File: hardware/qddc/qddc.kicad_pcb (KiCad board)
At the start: 2 copper layers, 37 parts, among them IC1 FST3253MTCX, IC2 OPA2350UA, J1 In_cos, J2 In_sin, J3 In_RF, J4 PWR, J5 Out_I, J6 Out_Q, T1 ETC4-1-2TR

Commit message: PCB for Quad DDC
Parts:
- C4: moved to B.Cu
- moved J5 20.3 mm to (164.5, 94.6)
- moved J6 20.3 mm to (164.5, 112.4)
- moved R10 17.2 mm to (123.8, 113.0), turned to 90 degrees
- moved R14 16.5 mm to (133.3, 111.8), turned to 90 degrees
- moved C10 15.6 mm to (135.9, 111.8), turned to 270 degrees
- moved C6 15.2 mm to (120.7, 113.0)
- moved J2 13.5 mm to (114.9, 86.4)
- moved R2 13.5 mm to (114.9, 93.3)
- moved J1 13.5 mm to (134.0, 86.4)
- moved R1 13.5 mm to (134.0, 93.3)
- moved R8 13.4 mm to (127.6, 97.8), turned to 270 degrees
- moved C5 11.5 mm to (124.5, 97.8), turned to 270 degrees
- moved L1 9.67 mm to (119.4, 123.2)
- moved C12 9.53 mm to (156.2, 94.6), turned to 180 degrees
- moved C13 9.53 mm to (156.2, 112.4)
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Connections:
- IC2 pad 6: Net-(C10-Pad2) -> Net-(C10-Pad1)
- IC2 pad 7: Net-(C10-Pad1) -> Net-(C10-Pad2)
- J4 pad 1: PTT -> GND
- J4 pad 4: GND -> PTT
- R10 pad 1: Net-(C10-Pad2) -> Net-(C10-Pad1)
- R13 pad 2: Net-(C10-Pad1) -> Net-(C10-Pad2)
- R14 pad 1: Net-(C10-Pad1) -> Net-(C10-Pad2)
- R14 pad 2: Net-(C10-Pad2) -> Net-(C10-Pad1)
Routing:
- net PTT: track 0.00 -> 32.0 mm, vias 0 -> 3
- net VCC: track 0.00 -> 31.3 mm, vias 0 -> 2
- net Net-(C8-Pad1): track 0.00 -> 28.7 mm
- net VAA: track 0.00 -> 27.0 mm, vias 0 -> 2
- net Net-(C9-Pad2): track 0.00 -> 26.9 mm
- net Net-(C10-Pad1): track 0.00 -> 23.7 mm
- net Net-(C10-Pad2): track 0.00 -> 23.0 mm
- net Net-(C5-Pad2): track 0.00 -> 21.8 mm
- net Net-(C1-Pad1): track 0.00 -> 21.8 mm
- net Net-(C6-Pad1): track 0.00 -> 21.7 mm
- net Net-(C7-Pad2): track 0.00 -> 21.3 mm, vias 0 -> 2
- net Net-(J3-Pad2): track 0.00 -> 21.1 mm, vias 0 -> 2
- net Net-(IC1-Pad2): track 0.00 -> 18.6 mm, vias 0 -> 2
- net Net-(IC1-Pad14): track 0.00 -> 18.0 mm, vias 0 -> 2
- net Net-(C9-Pad1): track 0.00 -> 11.4 mm
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- added copper zone on B.Cu, net GND
- added copper zone on F.Cu, net GND
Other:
- board outline added: 71.1 x 46.4 mm

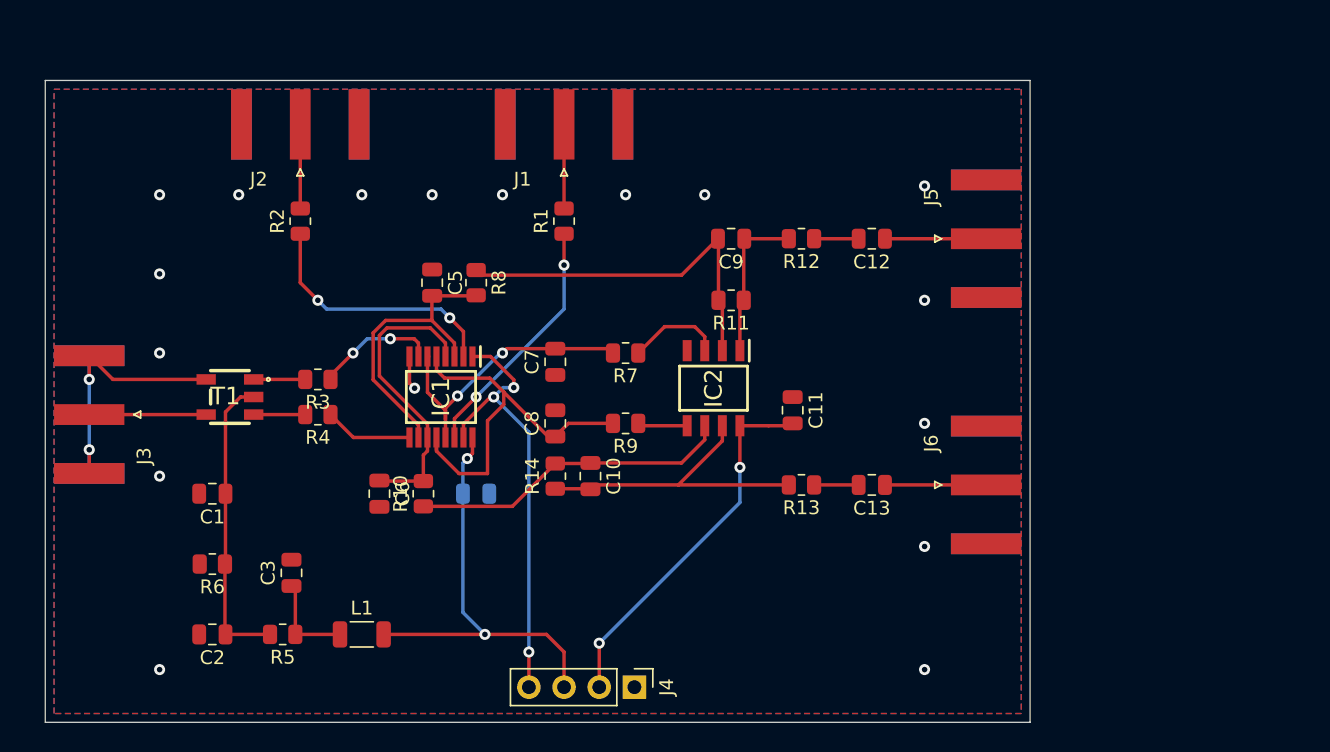
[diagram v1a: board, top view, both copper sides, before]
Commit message: Done PCB for Quad DDC
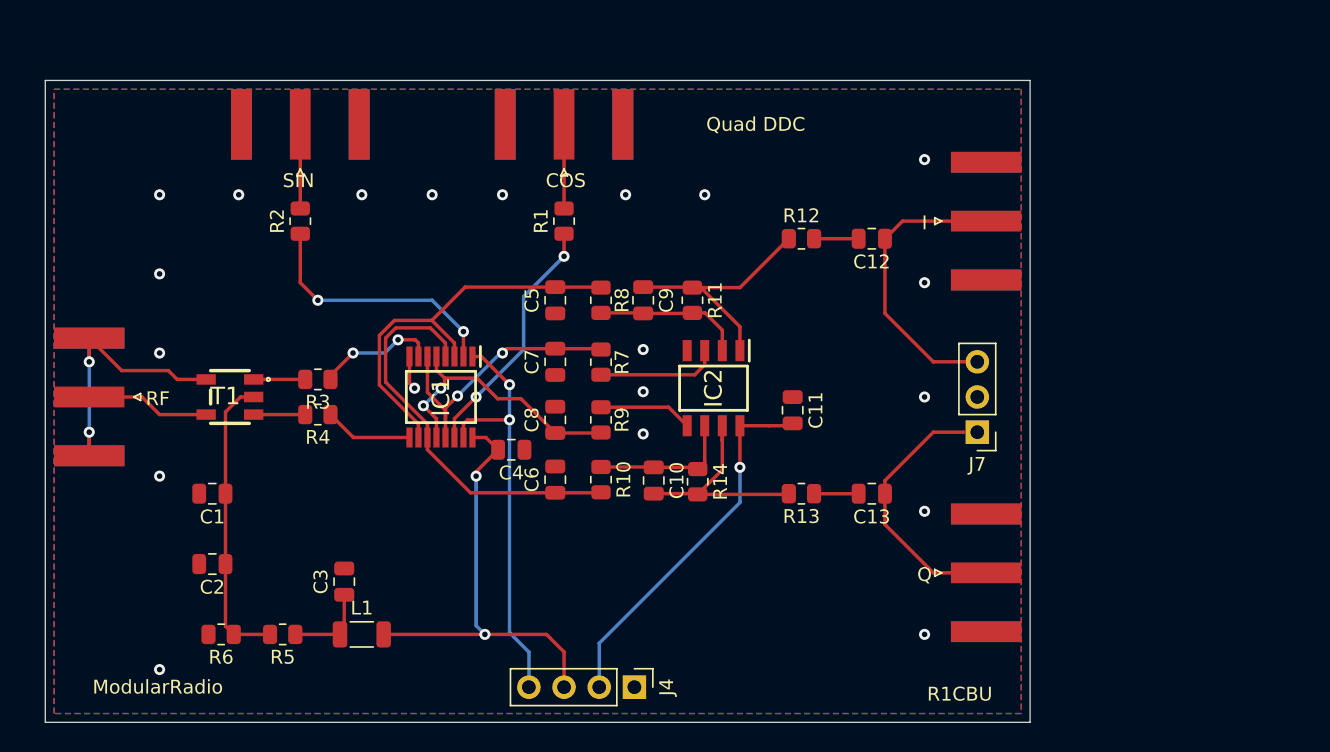
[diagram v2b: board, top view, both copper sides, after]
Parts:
- added J7: Conn_01x03_Male, Connector_PinHeader_2.54mm:PinHeader_1x03_P2.54mm_Vertical, F.Cu at (163.8, 108.6)
- C4: moved to F.Cu
- moved R10 12.9 mm to (136.7, 112.0), turned to 270 degrees
- moved C6 12.7 mm to (133.3, 112.0), turned to 90 degrees
- moved R14 10.3 mm to (143.6, 112.2)
- moved R8 9.11 mm to (136.7, 99.1), turned to 90 degrees
- moved C5 8.98 mm to (133.3, 99.1), turned to 90 degrees
- moved C9 7.75 mm to (139.7, 99.1), turned to 270 degrees
- moved Q 6.35 mm to (164.5, 118.7)
- moved R6 5.12 mm to (109.2, 123.2)
- moved C2 5.08 mm to (108.6, 118.1)
- moved C10 4.58 mm to (140.5, 112.1)
- moved C4 4.07 mm to (130.2, 109.9)
- moved C3 3.86 mm to (118.1, 119.4)
- moved R11 2.79 mm to (143.3, 99.1), turned to 270 degrees
- moved R7 1.90 mm to (136.7, 103.5), turned to 90 degrees
- moved R9 1.80 mm to (136.7, 107.7), turned to 270 degrees
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- renumbered J1 to COS, J5 to I, J6 to Q, J3 to RF, J2 to SIN
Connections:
- R12 pad 1: Net-(C12-Pad2) -> Net-(C9-Pad1)
- R12 pad 2: Net-(C9-Pad1) -> Net-(C12-Pad2)
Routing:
- net Net-(C9-Pad2): track 26.9 -> 10.8 mm
- net Net-(C12-Pad1): track 7.31 -> 21.3 mm
- net Net-(C10-Pad1): track 23.7 -> 10.8 mm
- net Net-(C13-Pad1): track 7.31 -> 20.0 mm
- net Net-(C8-Pad1): track 28.7 -> 20.1 mm, vias 0 -> 2
- net Net-(C6-Pad1): track 21.7 -> 29.2 mm
- net Net-(C5-Pad2): track 21.8 -> 29.3 mm
- net Net-(C9-Pad1): track 11.4 -> 18.3 mm
- net Net-(C10-Pad2): track 23.0 -> 16.6 mm
- net Net-(IC2-Pad5): track 3.85 -> 7.02 mm
- net Net-(IC2-Pad3): track 6.90 -> 8.81 mm
- net PTT: track 32.0 -> 30.4 mm, vias 3 -> 2
- net VCC: track 31.3 -> 32.6 mm
- net Net-(C7-Pad2): track 21.3 -> 20.3 mm
- net Net-(C3-Pad1): track 6.84 -> 6.21 mm
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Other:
- board text added: "ModularRadio"
- board text added: "Quad DDC"
- board text added: "R1CBU"

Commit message: Optimize Quad DDC, Gerber files
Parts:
- removed I: Out_I, Connector_Coaxial:SMA_Amphenol_132289_EdgeMount
- removed Q: Out_Q, Connector_Coaxial:SMA_Amphenol_132289_EdgeMount
- removed the RF at (99.7, 106.0)
- added RF: In_RF, kicad:RFSOLUTIONS_CON-SMA-EDGE-S, F.Cu at (104.1, 104.6)
- Cos: renamed from COS; footprint Connector_Coaxial:SMA_Amphenol_132289_EdgeMount -> kicad:RFSOLUTIONS_CON-SMA-EDGE-S
- Sin: renamed from SIN; footprint Connector_Coaxial:SMA_Amphenol_132289_EdgeMount -> kicad:RFSOLUTIONS_CON-SMA-EDGE-S
- moved R6 22.7 mm to (111.8, 100.6)
- moved Out 10.8 mm to (153.0, 108.0)
- moved L1 9.73 mm to (125.7, 115.8)
- moved R5 8.02 mm to (116.8, 115.8)
- moved Cos 7.91 mm to (126.5, 88.9), turned to 270 degrees
- moved PWR 7.63 mm to (138.7, 119.4)
- moved R1 7.52 mm to (126.5, 94.0)
- moved C12 5.85 mm to (151.8, 98.4)
- moved R12 5.39 mm to (147.3, 98.4)
- moved C3 5.12 mm to (120.7, 114.9)
- moved C13 4.45 mm to (151.8, 113.0)
- moved C2 3.91 mm to (111.8, 115.8)
- moved R13 3.81 mm to (147.3, 113.0)
- moved C1 3.64 mm to (111.8, 111.3)
- moved Sin 2.57 mm to (115.3, 88.9), turned to 270 degrees
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- renumbered J7 to Out, J4 to PWR
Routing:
- net Net-(C12-Pad1): track 21.3 -> 4.58 mm
- net VCC: track 32.6 -> 16.4 mm
- net Net-(C13-Pad1): track 20.0 -> 5.21 mm
- net Net-(J3-Pad1): track 21.6 -> 6.95 mm, vias 2 -> 0
- net Net-(J3-PadG1): track 8.97 -> 22.1 mm, vias 0 -> 2
- net VAA: track 27.0 -> 19.9 mm
- net PTT: track 30.4 -> 23.5 mm
- net Net-(C9-Pad1): track 18.3 -> 13.2 mm
- net Net-(C10-Pad2): track 16.6 -> 12.2 mm
- net Net-(IC1-Pad2): track 18.6 -> 15.9 mm
- net Net-(IC1-Pad9): track 6.39 -> 4.48 mm
- net Net-(J2-Pad1): track 6.07 -> 4.23 mm
- net Net-(C1-Pad1): track 21.4 -> 19.8 mm
- net Net-(J1-Pad1): track 6.07 -> 4.46 mm
- net Net-(IC1-Pad7): track 8.77 -> 7.24 mm
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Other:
- board size 71.1 x 46.4 mm -> 54 x 35.6 mm
